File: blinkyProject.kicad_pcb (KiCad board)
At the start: 2 copper layers, 28 x 28 mm, 14 parts, among them J1 USB_B_Micro, J2 Conn_02x10_Odd_Even, U1 stm32f030, U2 LD1117S33TR_SOT223

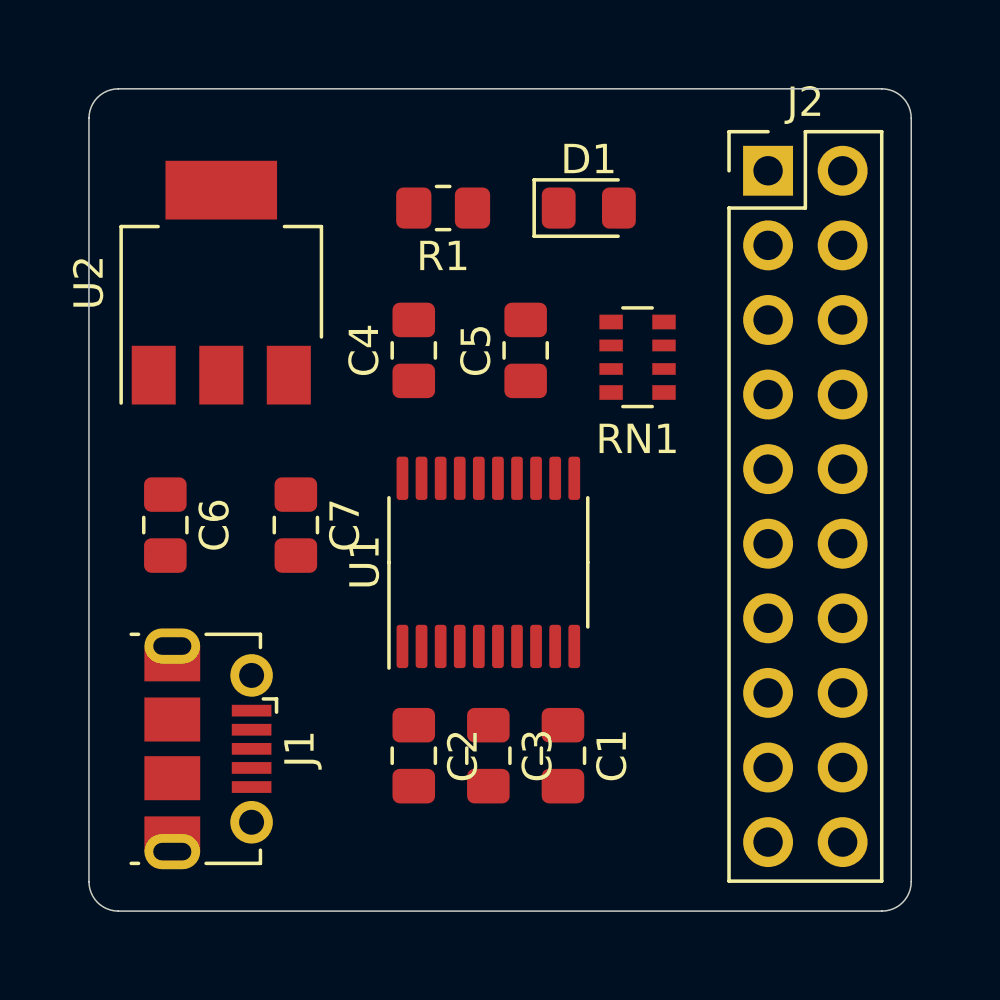
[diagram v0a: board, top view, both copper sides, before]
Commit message: Completes routing
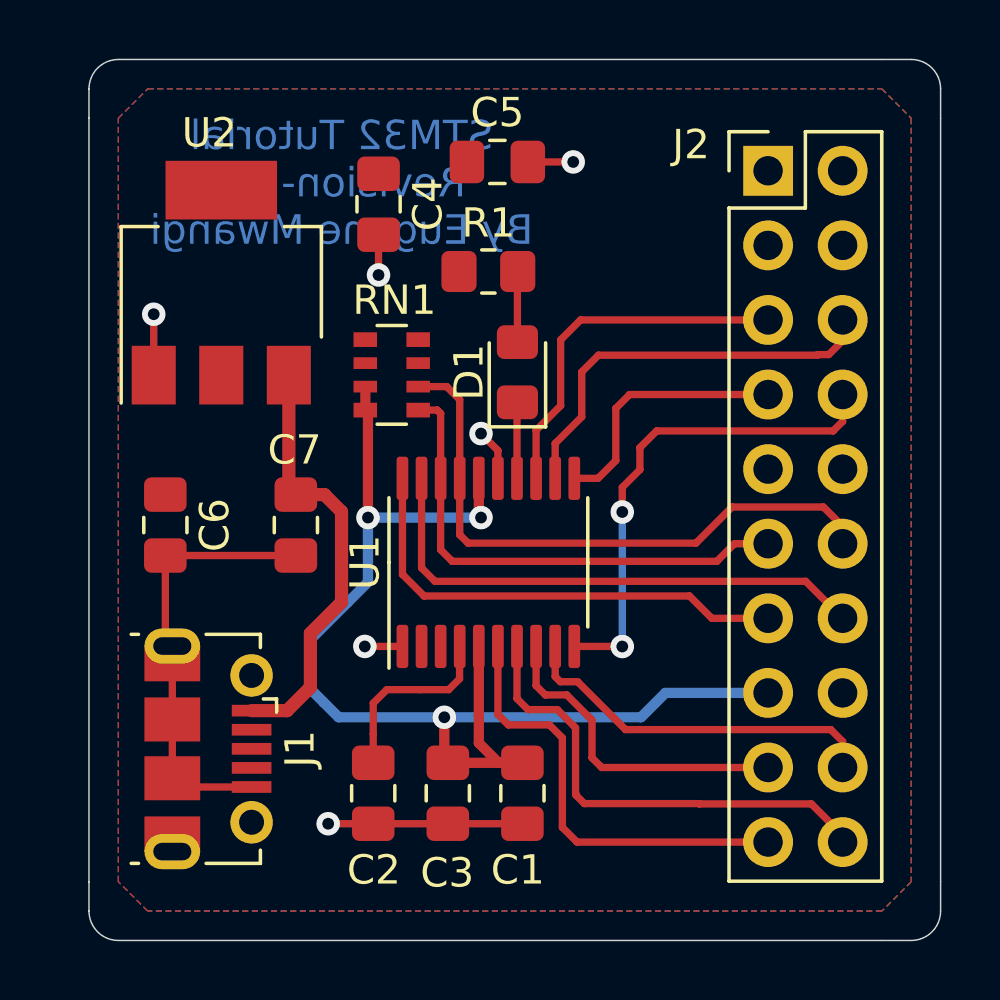
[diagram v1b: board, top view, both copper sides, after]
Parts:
- moved RN1 8.39 mm to (98.3, 104.7)
- moved C5 6.49 mm to (101.9, 97.5), turned to 0 degrees
- moved D1 6.10 mm to (102.6, 104.7), turned to 90 degrees
- moved C4 5.12 mm to (97.9, 98.9), turned to 270 degrees
- moved R1 2.65 mm to (101.6, 101.2), turned to 0 degrees
- moved C1 1.88 mm to (102.8, 119.0)
- moved C2 1.88 mm to (97.7, 119.0)
- moved C3 1.88 mm to (100.2, 119.0)
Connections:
- J2 pad 10: SPI1_NSS -> GND
- J2 pad 11: +3V3 -> I2C1_SDA
- J2 pad 12: SPI1_SCK -> I2C1_SCL
- J2 pad 13: ADC_IN0 -> SWCLK
- J2 pad 14: SPI1_MISO -> SWDIO
- J2 pad 15: ADC_IN1 -> +3V3
- J2 pad 16: SPI1_MOSI -> GND
- J2 pad 17: GND -> USART1_TX
- J2 pad 18: USART1_TX -> USART1_RX
- J2 pad 19: GND -> ADC_IN0
- J2 pad 2: SWDIO -> GND
- J2 pad 20: USART1_RX -> ADC_IN1
- J2 pad 3: GND -> +3V3
- J2 pad 4: SWCLK -> GND
- J2 pad 5: GND -> SPI1_MOSI
- J2 pad 6: I2C1_SCL -> SPI1_MISO
- J2 pad 7: Net-(J2-Pad7) -> SPI1_SCK
- J2 pad 8: I2C1_SDA -> SPI1_NSS
- J2 pad 9: +3V3 -> GND
- RN1 pad 1: I2C1_SCL -> I2C1_SDA
- RN1 pad 2: I2C1_SDA -> I2C1_SCL
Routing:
- net +3V3: track 0.00 -> 42.4 mm, vias 0 -> 3
- net GND: track 0.00 -> 29.6 mm, vias 0 -> 6
- net I2C1_SCL: track 0.00 -> 20.7 mm
- net SWDIO: track 0.00 -> 18.1 mm
- net I2C1_SDA: track 0.00 -> 17.1 mm
- net SPI1_NSS: track 0.00 -> 16.8 mm, vias 0 -> 2
- net ADC_IN1: track 0.00 -> 16.4 mm
- net SWCLK: track 0.00 -> 16.3 mm
- net ADC_IN0: track 0.00 -> 15.1 mm
- net +5V: track 0.00 -> 14.8 mm
- net SPI1_MISO: track 0.00 -> 14.0 mm
- net USART1_RX: track 0.00 -> 12.6 mm
- net SPI1_MOSI: track 0.00 -> 12.4 mm
- net USART1_TX: track 0.00 -> 11.1 mm
- net SPI1_SCK: track 0.00 -> 8.82 mm
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- added copper zone on F.Cu, net +3V3
- added copper zone on B.Cu, net GND
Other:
- board size 28 x 28 mm -> 29 x 30 mm
- net class 5V added: clearance 0.2, trace_width 0.45, via_dia 0.8, via_drill 0.4
- net class power added: clearance 0.2, trace_width 0.35, via_dia 0.8, via_drill 0.4
- board text added: "STM32 Tutorial Revision-1.0 By Eugene Mwangi"

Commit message: Closes the pcb brd file
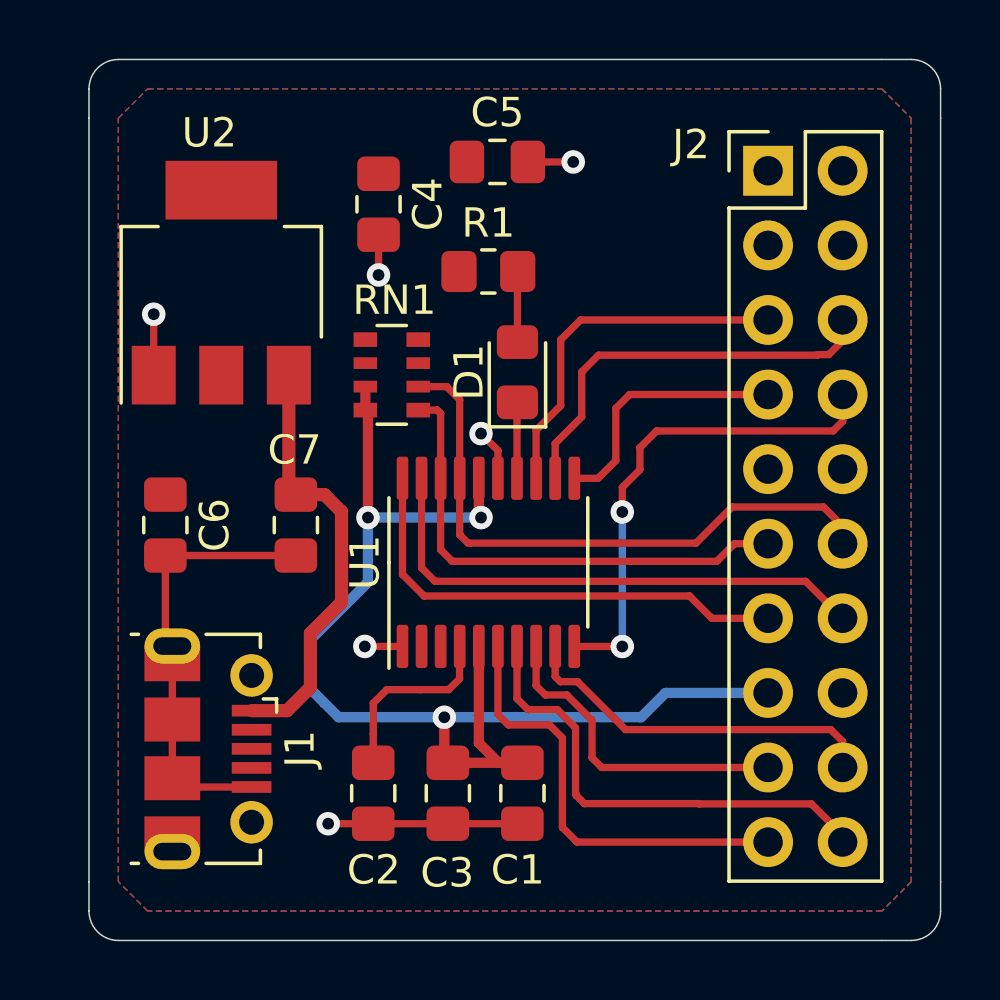
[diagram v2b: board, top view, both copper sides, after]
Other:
- board text added: "STM32 Tutorial Revision-1.0 By Eugene"
- board text removed: "STM32 Tutorial Revision-1.0 By Eugene Mwangi"
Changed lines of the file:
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@@
       (outputformat 1)
       (mirror false)
-      (drillshape 1)
+      (drillshape 0)
       (scaleselection 1)
       (outputdirectory ""))
@@
       (effects (font (size 0.5 0.5) (thickness 0.08)))
     )
-    (pad 2 smd roundrect (at 1.0375 0 270) (size 1.175 1.45) (layers F.Cu F.Paste F.Mask) (roundrect_rratio 0.212766)
-      (net 1 GND))
-    (pad 1 smd roundrect (at -1.0375 0 270) (size 1.175 1.45) (layers F.Cu F.Paste F.Mask) (roundrect_rratio 0.212766)
+    (pad 2 smd roundrect (at 1.0375 0 270) (size 1.175 1.45) (layers F.Cu F.Paste F.Mask) (roundrect_rratio 0.2127659574468085)
+      (net 1 GND))
+    (pad 1 smd roundrect (at -1.0375 0 270) (size 1.175 1.45) (layers F.Cu F.Paste F.Mask) (roundrect_rratio 0.2127659574468085)
       (net 2 +3V3))
     (model ${KISYS3DMOD}/Capacitor_SMD.3dshapes/C_0805_2012Metric.wrl
@@
       (effects (font (size 0.5 0.5) (thickness 0.08)))
     )
-    (pad 2 smd roundrect (at 1.0375 0 270) (size 1.175 1.45) (layers F.Cu F.Paste F.Mask) (roundrect_rratio 0.212766)
-      (net 1 GND))
-    (pad 1 smd roundrect (at -1.0375 0 270) (size 1.175 1.45) (layers F.Cu F.Paste F.Mask) (roundrect_rratio 0.212766)
+    (pad 2 smd roundrect (at 1.0375 0 270) (size 1.175 1.45) (layers F.Cu F.Paste F.Mask) (roundrect_rratio 0.2127659574468085)
+      (net 1 GND))
+    (pad 1 smd roundrect (at -1.0375 0 270) (size 1.175 1.45) (layers F.Cu F.Paste F.Mask) (roundrect_rratio 0.2127659574468085)
       (net 27 +5V))
     (model ${KISYS3DMOD}/Capacitor_SMD.3dshapes/C_0805_2012Metric.wrl
@@
       (effects (font (size 0.5 0.5) (thickness 0.08)))
     )
-    (pad 2 smd roundrect (at 1.0375 0 270) (size 1.175 1.45) (layers F.Cu F.Paste F.Mask) (roundrect_rratio 0.212766)
-      (net 1 GND))
-    (pad 1 smd roundrect (at -1.0375 0 270) (size 1.175 1.45) (layers F.Cu F.Paste F.Mask) (roundrect_rratio 0.212766)
+    (pad 2 smd roundrect (at 1.0375 0 270) (size 1.175 1.45) (layers F.Cu F.Paste F.Mask) (roundrect_rratio 0.2127659574468085)
+      (net 1 GND))
+    (pad 1 smd roundrect (at -1.0375 0 270) (size 1.175 1.45) (layers F.Cu F.Paste F.Mask) (roundrect_rratio 0.2127659574468085)
       (net 2 +3V3))
     (model ${KISYS3DMOD}/Capacitor_SMD.3dshapes/C_0805_2012Metric.wrl
@@
       (effects (font (size 0.5 0.5) (thickness 0.08)))
     )
-    (pad 1 smd roundrect (at -1.0375 0 270) (size 1.175 1.45) (layers F.Cu F.Paste F.Mask) (roundrect_rratio 0.212766)
+    (pad 1 smd roundrect (at -1.0375 0 270) (size 1.175 1.45) (layers F.Cu F.Paste F.Mask) (roundrect_rratio 0.2127659574468085)
       (net 3 NRST))
-    (pad 2 smd roundrect (at 1.0375 0 270) (size 1.175 1.45) (layers F.Cu F.Paste F.Mask) (roundrect_rratio 0.212766)
+    (pad 2 smd roundrect (at 1.0375 0 270) (size 1.175 1.45) (layers F.Cu F.Paste F.Mask) (roundrect_rratio 0.2127659574468085)
       (net 1 GND))
     (model ${KISYS3DMOD}/Capacitor_SMD.3dshapes/C_0805_2012Metric.wrl
@@
       (effects (font (size 0.5 0.5) (thickness 0.08)))
     )
-    (pad 2 smd roundrect (at 1.0375 0 270) (size 1.175 1.45) (layers F.Cu F.Paste F.Mask) (roundrect_rratio 0.212766)
-      (net 1 GND))
-    (pad 1 smd roundrect (at -1.0375 0 270) (size 1.175 1.45) (layers F.Cu F.Paste F.Mask) (roundrect_rratio 0.212766)
+    (pad 2 smd roundrect (at 1.0375 0 270) (size 1.175 1.45) (layers F.Cu F.Paste F.Mask) (roundrect_rratio 0.2127659574468085)
+      (net 1 GND))
+    (pad 1 smd roundrect (at -1.0375 0 270) (size 1.175 1.45) (layers F.Cu F.Paste F.Mask) (roundrect_rratio 0.2127659574468085)
       (net 2 +3V3))
     (model ${KISYS3DMOD}/Capacitor_SMD.3dshapes/C_0805_2012Metric.wrl
@@
       (effects (font (size 0.5 0.5) (thickness 0.08)))
     )
-    (pad 1 smd roundrect (at -1.0375 0 270) (size 1.175 1.45) (layers F.Cu F.Paste F.Mask) (roundrect_rratio 0.212766)
-      (net 2 +3V3))
-    (pad 2 smd roundrect (at 1.0375 0 270) (size 1.175 1.45) (layers F.Cu F.Paste F.Mask) (roundrect_rratio 0.212766)
+    (pad 1 smd roundrect (at -1.0375 0 270) (size 1.175 1.45) (layers F.Cu F.Paste F.Mask) (roundrect_rratio 0.2127659574468085)
+      (net 2 +3V3))
+    (pad 2 smd roundrect (at 1.0375 0 270) (size 1.175 1.45) (layers F.Cu F.Paste F.Mask) (roundrect_rratio 0.2127659574468085)
       (net 1 GND))
     (model ${KISYS3DMOD}/Capacitor_SMD.3dshapes/C_0805_2012Metric.wrl
@@
       (effects (font (size 0.5 0.5) (thickness 0.08)))
     )
-    (pad 1 smd roundrect (at -1.0375 0) (size 1.175 1.45) (layers F.Cu F.Paste F.Mask) (roundrect_rratio 0.212766)
-      (net 2 +3V3))
-    (pad 2 smd roundrect (at 1.0375 0) (size 1.175 1.45) (layers F.Cu F.Paste F.Mask) (roundrect_rratio 0.212766)
+    (pad 1 smd roundrect (at -1.0375 0) (size 1.175 1.45) (layers F.Cu F.Paste F.Mask) (roundrect_rratio 0.2127659574468085)
+      (net 2 +3V3))
+    (pad 2 smd roundrect (at 1.0375 0) (size 1.175 1.45) (layers F.Cu F.Paste F.Mask) (roundrect_rratio 0.2127659574468085)
       (net 1 GND))
     (model ${KISYS3DMOD}/Capacitor_SMD.3dshapes/C_0805_2012Metric.wrl
@@
       (effects (font (size 0.5 0.5) (thickness 0.08)))
     )
-    (pad 1 smd roundrect (at -1.025 0 90) (size 1.15 1.4) (layers F.Cu F.Paste F.Mask) (roundrect_rratio 0.217391)
+    (pad 1 smd roundrect (at -1.025 0 90) (size 1.15 1.4) (layers F.Cu F.Paste F.Mask) (roundrect_rratio 0.2173904347826087)
       (net 4 "Net-(D1-Pad1)"))
-    (pad 2 smd roundrect (at 1.025 0 90) (size 1.15 1.4) (layers F.Cu F.Paste F.Mask) (roundrect_rratio 0.217391)
+    (pad 2 smd roundrect (at 1.025 0 90) (size 1.15 1.4) (layers F.Cu F.Paste F.Mask) (roundrect_rratio 0.2173904347826087)
       (net 5 "Net-(D1-Pad2)"))
     (model ${KISYS3DMOD}/LED_SMD.3dshapes/LED_0805_2012Metric.wrl
@@
       (effects (font (size 0.5 0.5) (thickness 0.08)))
     )
-    (pad 1 smd roundrect (at -1 0) (size 1.2 1.4) (layers F.Cu F.Paste F.Mask) (roundrect_rratio 0.208333)
-      (net 2 +3V3))
-    (pad 2 smd roundrect (at 1 0) (size 1.2 1.4) (layers F.Cu F.Paste F.Mask) (roundrect_rratio 0.208333)
+    (pad 1 smd roundrect (at -1 0) (size 1.2 1.4) (layers F.Cu F.Paste F.Mask) (roundrect_rratio 0.2083325)
+      (net 2 +3V3))
+    (pad 2 smd roundrect (at 1 0) (size 1.2 1.4) (layers F.Cu F.Paste F.Mask) (roundrect_rratio 0.2083325)
       (net 5 "Net-(D1-Pad2)"))
     (model ${KISYS3DMOD}/Resistor_SMD.3dshapes/R_0805_2012Metric.wrl
@@
     )
   )
-  (gr_text "STM32 Tutorial\nRevision-1.0\nBy Eugene Mwangi" (at 96.6 98.2) (layer B.Cu)
+  (gr_text "STM32 Tutorial\nRevision-1.0\nBy Eugene" (at 95.8 98.3) (layer B.SilkS)
     (effects (font (size 1 1) (thickness 0.15)) (justify mirror))
   )
